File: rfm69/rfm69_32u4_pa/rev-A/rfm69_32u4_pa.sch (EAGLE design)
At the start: 125 parts, among them IC1 ATMEGA32U4-AU, IC2 74HC04D, IC3 MCP9700, SW1 HMC284AMS8G, SW1A TPSQTP10SQ, SW1B TPSQTP10SQ, SW2 HMC574AMS8E, SW2A TPSQTP10SQ, SW2B TPSQTP10SQ, Y1 8MHz

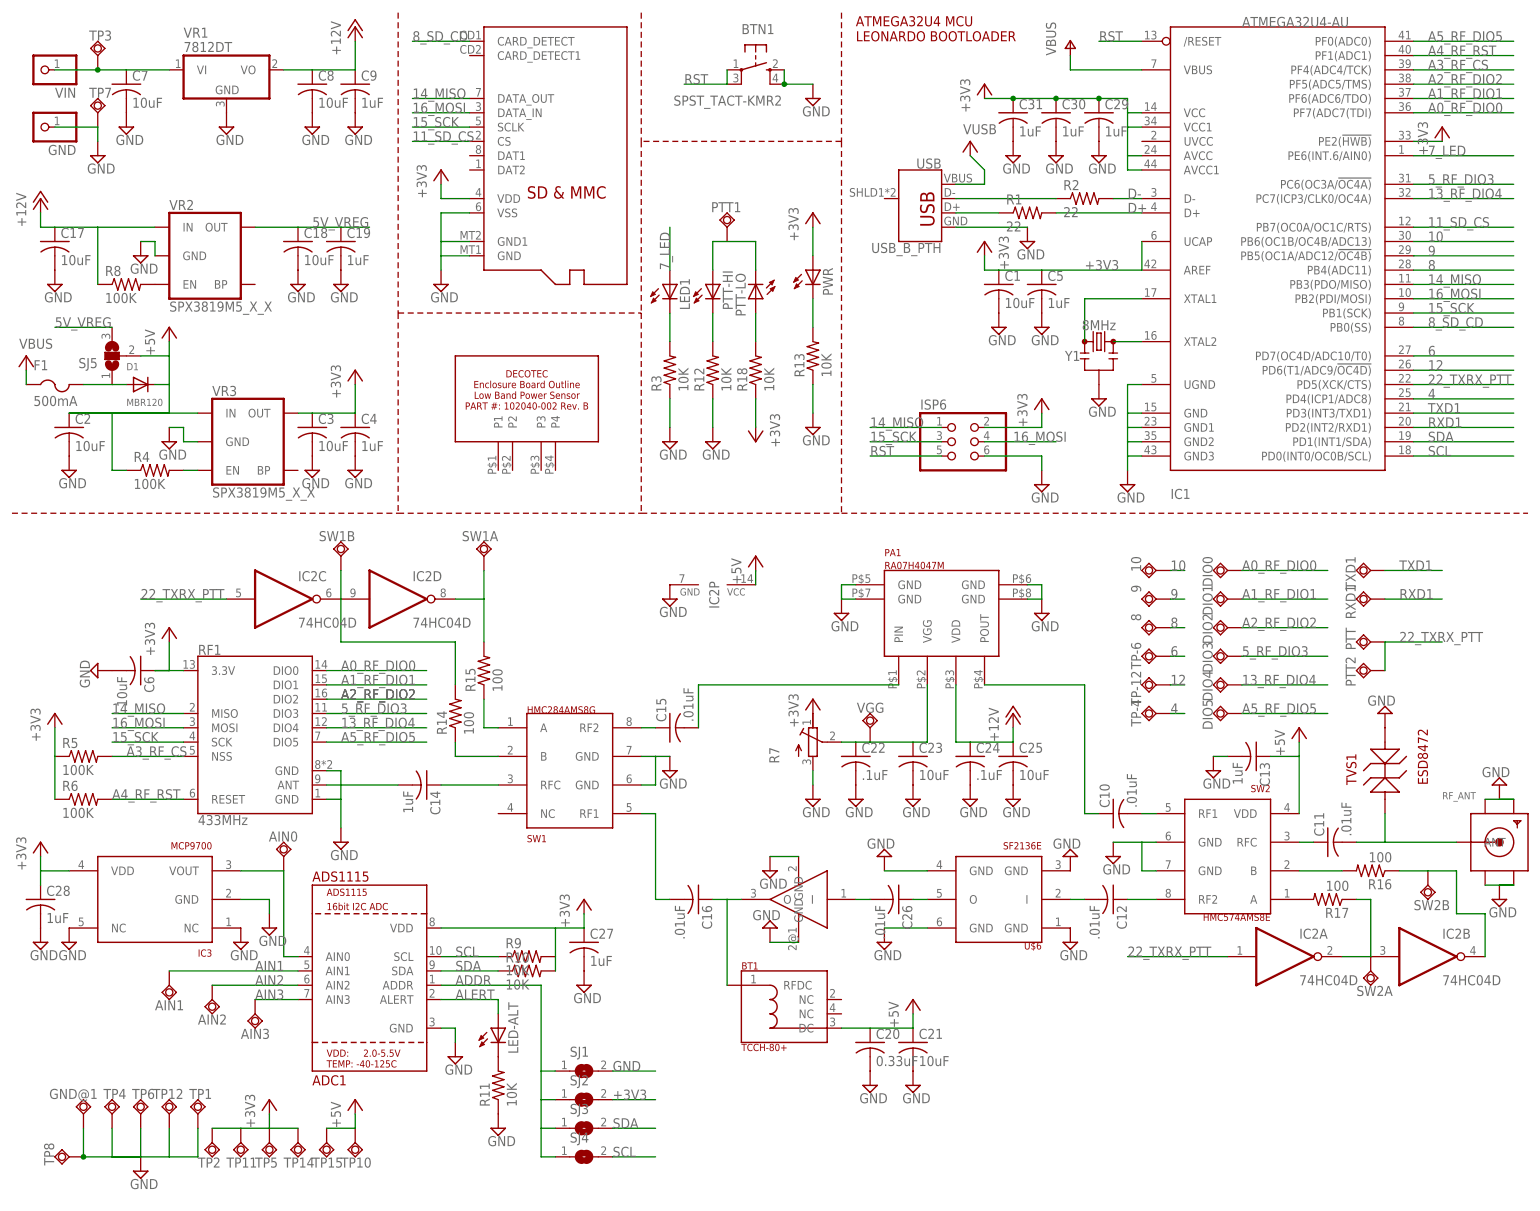
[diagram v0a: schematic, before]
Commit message: Changed PTT pin from physical pin 22 to physical pin 25 which is mapped to arduino digital pin 4.  This was done because there is no mapping of physical pin 22 to an arduino digital pin for the feather32u4.
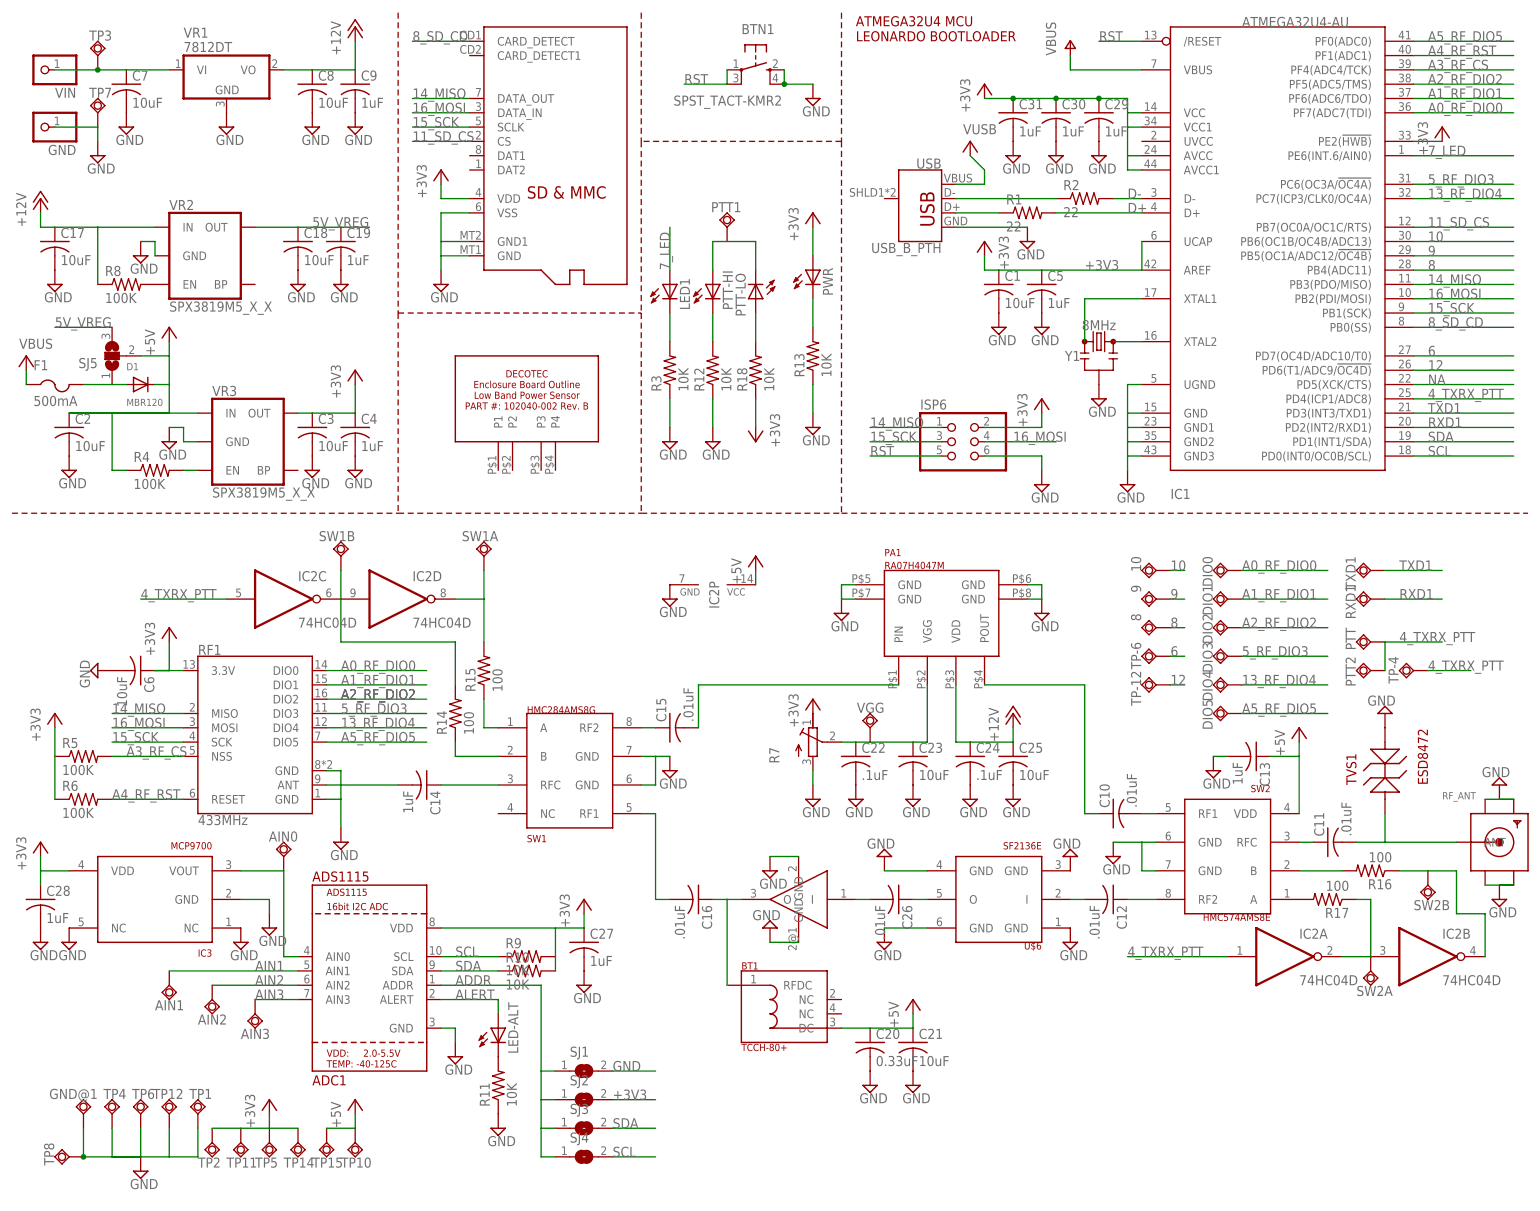
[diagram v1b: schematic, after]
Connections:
- removed net 22_TXRX_PTT: IC1.PD5(XCK/CTS), IC2A.I, IC2C.I, PTT.TP, PTT2.TP
- removed net 4: IC1.PD4(ICP1/ADC8), TP-4.TP
- new net 4_TXRX_PTT: IC1.PD4(ICP1/ADC8), IC2A.I, IC2C.I, PTT.TP, PTT2.TP, TP-4.TP
- new net NA: IC1.PD5(XCK/CTS)
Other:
- moved on the sheet: TP-4
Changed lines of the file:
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@@
 <instance part="TP-6" gate="G$1" x="208.28" y="96.52" rot="R270"/>
 <instance part="TP-12" gate="G$1" x="208.28" y="91.44" rot="R270"/>
-<instance part="TP-4" gate="G$1" x="208.28" y="86.36" rot="R270"/>
+<instance part="TP-4" gate="G$1" x="254" y="93.98" rot="R270"/>
 <instance part="TP10" gate="G$1" x="66.04" y="10.16"/>
 <instance part="TP11" gate="G$1" x="45.72" y="10.16"/>
@@
 <net name="9" class="0">
 <segment>
+<pinref part="9" gate="G$1" pin="TP"/>
+<wire x1="210.82" y1="106.68" x2="213.36" y2="106.68" width="0.1524" layer="91"/>
+<label x="210.82" y="106.68" size="1.778" layer="95"/>
+</segment>
+<segment>
 <pinref part="IC1" gate="G$1" pin="PB5(OC1A/ADC12/!OC4B)"/>
 <wire x1="254" y1="167.64" x2="271.78" y2="167.64" width="0.1524" layer="91"/>
 <label x="256.54" y="167.64" size="1.778" layer="95"/>
-</segment>
-<segment>
-<pinref part="9" gate="G$1" pin="TP"/>
-<wire x1="210.82" y1="106.68" x2="213.36" y2="106.68" width="0.1524" layer="91"/>
-<label x="210.82" y="106.68" size="1.778" layer="95"/>
 </segment>
 </net>
@@
 <wire x1="86.36" y1="187.96" x2="76.2" y2="187.96" width="0.1524" layer="91"/>
 <label x="76.2" y="187.96" size="1.778" layer="95"/>
-</segment>
-</net>
-<net name="4" class="0">
-<segment>
-<pinref part="IC1" gate="G$1" pin="PD4(ICP1/ADC8)"/>
-<wire x1="254" y1="142.24" x2="271.78" y2="142.24" width="0.1524" layer="91"/>
-<label x="256.54" y="142.24" size="1.778" layer="95"/>
-</segment>
-<segment>
-<pinref part="TP-4" gate="G$1" pin="TP"/>
-<wire x1="210.82" y1="86.36" x2="213.36" y2="86.36" width="0.1524" layer="91"/>
-<label x="210.82" y="86.36" size="1.778" layer="95"/>
 </segment>
 </net>
@@
 </segment>
 </net>
-<net name="22_TXRX_PTT" class="0">
-<segment>
-<pinref part="IC1" gate="G$1" pin="PD5(XCK/CTS)"/>
-<wire x1="254" y1="144.78" x2="271.78" y2="144.78" width="0.1524" layer="91"/>
-<label x="256.54" y="144.78" size="1.778" layer="95"/>
-</segment>
-<segment>
-<pinref part="IC2" gate="A" pin="I"/>
-<wire x1="220.98" y1="43.18" x2="203.2" y2="43.18" width="0.1524" layer="91"/>
-<label x="203.2" y="43.18" size="1.778" layer="95"/>
-</segment>
-<segment>
-<pinref part="IC2" gate="C" pin="I"/>
-<wire x1="43.18" y1="106.68" x2="27.94" y2="106.68" width="0.1524" layer="91"/>
-<label x="27.94" y="106.68" size="1.778" layer="95"/>
-</segment>
-<segment>
-<pinref part="PTT" gate="G$1" pin="TP"/>
-<wire x1="248.92" y1="99.06" x2="259.08" y2="99.06" width="0.1524" layer="91"/>
-<label x="251.46" y="99.06" size="1.778" layer="95"/>
-<pinref part="PTT2" gate="G$1" pin="TP"/>
-<wire x1="248.92" y1="93.98" x2="248.92" y2="99.06" width="0.1524" layer="91"/>
-</segment>
-</net>
 <net name="8_SD_CD" class="0">
 <segment>
@@
 </segment>
 </net>
+<net name="NA" class="0">
+<segment>
+<pinref part="IC1" gate="G$1" pin="PD5(XCK/CTS)"/>
+<wire x1="254" y1="144.78" x2="271.78" y2="144.78" width="0.1524" layer="91"/>
+<label x="256.54" y="144.78" size="1.778" layer="95"/>
+</segment>
+</net>
+<net name="4_TXRX_PTT" class="0">
+<segment>
+<pinref part="IC1" gate="G$1" pin="PD4(ICP1/ADC8)"/>
+<wire x1="254" y1="142.24" x2="271.78" y2="142.24" width="0.1524" layer="91"/>
+<label x="256.54" y="142.24" size="1.778" layer="95"/>
+</segment>
+<segment>
+<pinref part="PTT" gate="G$1" pin="TP"/>
+<wire x1="248.92" y1="99.06" x2="259.08" y2="99.06" width="0.1524" layer="91"/>
+<label x="251.46" y="99.06" size="1.778" layer="95"/>
+<pinref part="PTT2" gate="G$1" pin="TP"/>
+<wire x1="248.92" y1="93.98" x2="248.92" y2="99.06" width="0.1524" layer="91"/>
+</segment>
+<segment>
+<pinref part="TP-4" gate="G$1" pin="TP"/>
+<wire x1="256.54" y1="93.98" x2="264.16" y2="93.98" width="0.1524" layer="91"/>
+<label x="256.54" y="93.98" size="1.778" layer="95"/>
+</segment>
+<segment>
+<pinref part="IC2" gate="C" pin="I"/>
+<wire x1="43.18" y1="106.68" x2="27.94" y2="106.68" width="0.1524" layer="91"/>
+<label x="27.94" y="106.68" size="1.778" layer="95"/>
+</segment>
+<segment>
+<pinref part="IC2" gate="A" pin="I"/>
+<wire x1="220.98" y1="43.18" x2="203.2" y2="43.18" width="0.1524" layer="91"/>
+<label x="203.2" y="43.18" size="1.778" layer="95"/>
+</segment>
+</net>

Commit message: Final updates.  Final Gerbers submitted for fabrication.
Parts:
- removed AIN0, AIN1, AIN2, AIN3, DIO0, DIO1, DIO2, DIO3, DIO4, DIO5, GND@1, PTT, PTT1, PTT2, TP-12, TP-4, TP-6, TP10, TP11, TP12, TP14, TP15, TXD1: TPSQTP10SQ, testpad:TPSQTP10SQ
- removed LED-ALT, PTT-LO: (no value), adafruit:LEDCHIPLED_0805
- removed TVS1: ESD8472, kj4qlp:ESD8472
- added 12, 4, 6, A0, A1, A2, A3: TPSQTP10SQ, testpad:TPSQTP10SQ
- added C32: 1uF, rcl:C-USC0805K
- added LED-RX: (no value), adafruit:LEDCHIPLED_0805
- added R19: 100, adafruit:R-US_R0805
- added R20: 100k, adafruit:R-US_R0805
- added R21: 10k, adafruit:R-US_R0805
- added T1: (no value), transistor:MMBT3904LT1-NPN-SOT23-BEC
- added T2: (no value), transistor:MMBT3906LT1-PNP-SOT23-BEC
- added TP-GND, TP-VIN: TPSQTP20SQ, testpad:TPSQTP20SQ
- C14: value 1uF -> .01uF
- C21, C23, C25: value 10uF -> 22uF
- R11: value 10K -> 330
- R18: value 10K -> 3.3k
- TP3, TP7: value TPSQTP20SQ -> TPSQTP10SQ; device testpad:TPSQTP20SQ -> testpad:TPSQTP10SQ
- renumbered PTT-HI to LED-PTT
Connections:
- net RXD1 renamed 0_RX
- removed net 4_TXRX_PTT: IC1.PD4(ICP1/ADC8), IC2A.I, IC2C.I, PTT.TP, PTT2.TP, TP-4.TP
- removed net A0_RF_DIO0: DIO0.TP, IC1.PF7(ADC7(TDI), RF1.DIO0
- removed net N$27: PTT-LO.A, R18.2
- removed net N$5: LED-PTT.A, PTT-LO.C, PTT1.TP
- removed net TXD1: IC1.PD3(INT3/TXD1), TXD1.TP
- new net 1_RF_DIO0: IC1.PD3(INT3/TXD1), LED-RX.A, RF1.DIO0
- new net 4_PTT: 4.TP, IC1.PD4(ICP1/ADC8), IC2A.I, IC2C.I, IC2F.I, R20.1
- new net A0: IC1.PF7(ADC7(TDI)
- new net N$28: IC2E.I, IC2F.O, R21.2
- new net N$29: R18.2, R7.A
- new net N$30: T1.C, T2.B
- new net N$31: BT1.DC, C20.1, C21.1, T2.C
- new net N$32: R19.2, T1.E
- new net N$34: R21.1, T1.B
- new net PTT_LED: IC2E.O, LED-PTT.A, R18.1
- net +3V3: now also TP3.TP, TP4.TP; no longer R18.1, R7.E, TP11.TP, TP14.TP, TP2.TP
- net +5V: now also C32.1, T2.E, TP1.TP, TP2.TP; no longer BT1.DC, C20.1, C21.1, TP10.TP, TP15.TP
- net 12: now also 12.TP; no longer TP-12.TP
- net 13_RF_DIO4: no longer DIO4.TP
- net 5_RF_DIO3: no longer DIO3.TP
- net 6: now also 6.TP; no longer TP-6.TP
- net A1_RF_DIO1: no longer DIO1.TP
- net A2_RF_DIO2: no longer DIO2.TP
- net A5_RF_DIO5: no longer DIO5.TP
- net AIN1: now also A1.TP; no longer AIN1.TP
- net AIN2: now also A2.TP; no longer AIN2.TP
- net AIN3: now also A3.TP; no longer AIN3.TP
- net ALERT: no longer LED-ALT.A
- net GND: now also C32.2, R19.1, R20.2, R7.E, TP-GND.TP; no longer GND@1.TP, R7.A, TP1.TP, TP12.TP, TP4.TP, TVS1.P$2
- net N$11: no longer TVS1.P$1
- net N$24: now also LED-RX.C; no longer LED-ALT.C
- net VIN: now also TP-VIN.TP; no longer TP3.TP
- net V_PA_TEMP: now also A0.TP; no longer AIN0.TP
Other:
- moved on the sheet: 10, 8, 9, ADC1, BT1, C10, C11, C12, C13, C14, C15, C16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
